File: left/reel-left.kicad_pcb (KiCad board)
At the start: 2 copper layers, 143.2 x 92.7 mm, 49 parts, among them J1 Conn_01x02, SW1 SW_Push, SW10 SW_Push, SW11 SW_Push, SW12 SW_Push, SW13 SW_Push, SW14 SW_Push, SW15 SW_Push, SW16 SW_Push, SW17 SW_Push, SW18 SW_Push, SW19 SW_Push, SW2 SW_Push, SW20 SW_Push, SW21 RotaryEncoder, SW22 SW_SPDT, SW3 SW_Push, SW4 SW_Push, SW5 SW_Push, SW6 SW_Push, SW7 SW_Push, SW8 SW_Push, SW9 SW_Push

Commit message: Update left PCB layout
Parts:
- added D21: D, Diode_SMD:D_SOD-123, F.Cu at (205.5, 115.8)
- added D22: D, Diode_SMD:D_SOD-123, F.Cu at (204.2, 118.0)
- added SW24: SW_SPDT, Button_Switch_SMD:SW_SPDT_PCM12, B.Cu at (208.3, 99.0)
- added SW25: RotaryEncoder, reel:RotaryEncoder_BM10_3Pin, F.Cu at (214.3, 122.9)
- SW21: value RotaryEncoder -> SW_Push; footprint reel:RotaryEncoder_BM10_3Pin -> reel:SideTactSwitch_2pin
- SW22: value SW_SPDT -> SW_Push; footprint Button_Switch_SMD:SW_SPDT_PCM12 -> reel:SideTactSwitch_2pin; moved to F.Cu
- moved SW22 45.8 mm to (202.0, 144.4), turned to 150 degrees
- moved SW21 3.93 mm to (216.7, 118.9)
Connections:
- SW22 pad 1: unconnected-(SW22-A-Pad1) -> Col1
- SW22 pad 2: Net-(J1-Pin_1) -> Net-(D22-A)
- U1 pad 15: unconnected-(U1-NFC1_0.09-Pad15) -> Row4
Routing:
- net Col1: track 193.8 -> 235.3 mm, vias 3 -> 4
- net Net-(D22-A): track 0.00 -> 28.9 mm
- net Net-(D21-A): track 0.00 -> 13.2 mm, vias 0 -> 1
- net Row4: track 0.00 -> 2.77 mm
- net unconnected-(SW24-A-Pad1): track 0.00 -> 0.65 mm
- net unconnected-(SW22-A-Pad1): track 0.65 -> 0.00 mm
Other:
- board size 143.2 x 92.7 mm -> 145.2 x 95 mm

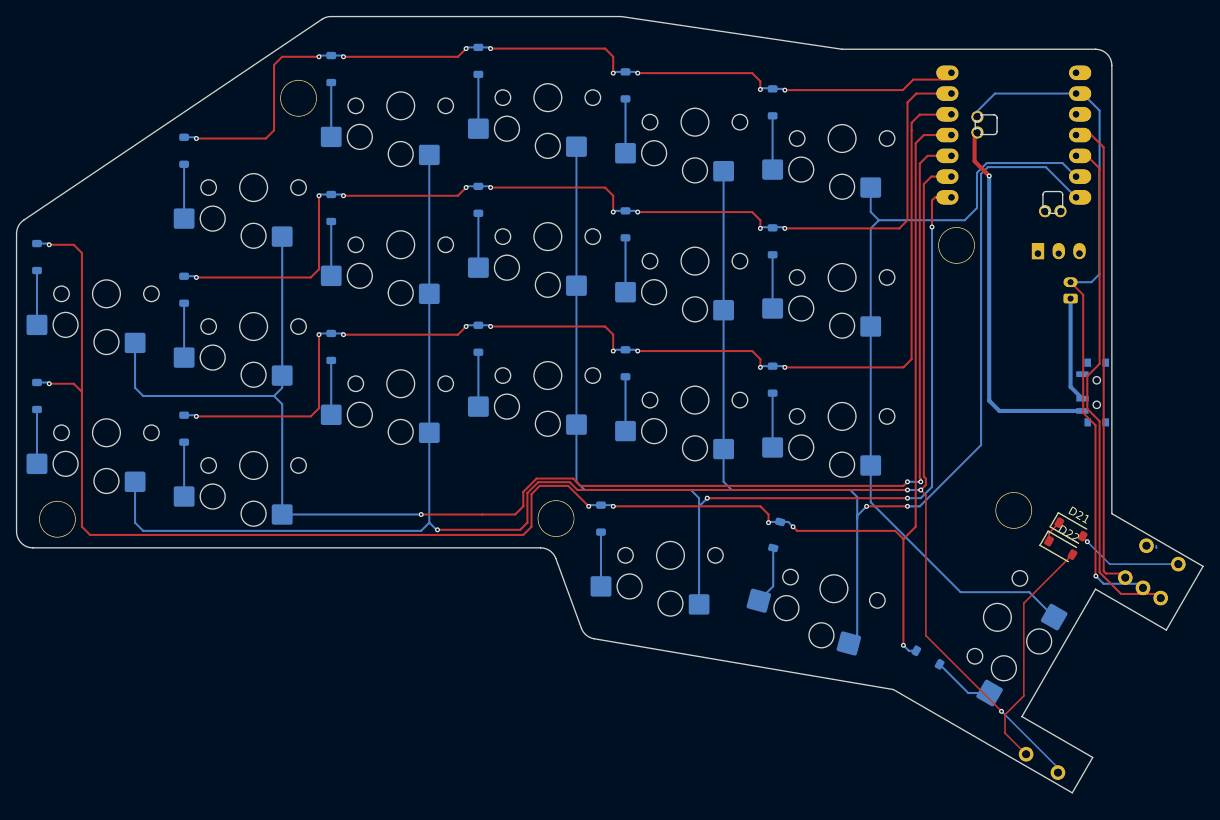
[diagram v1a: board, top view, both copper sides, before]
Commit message: Update left PCB layout
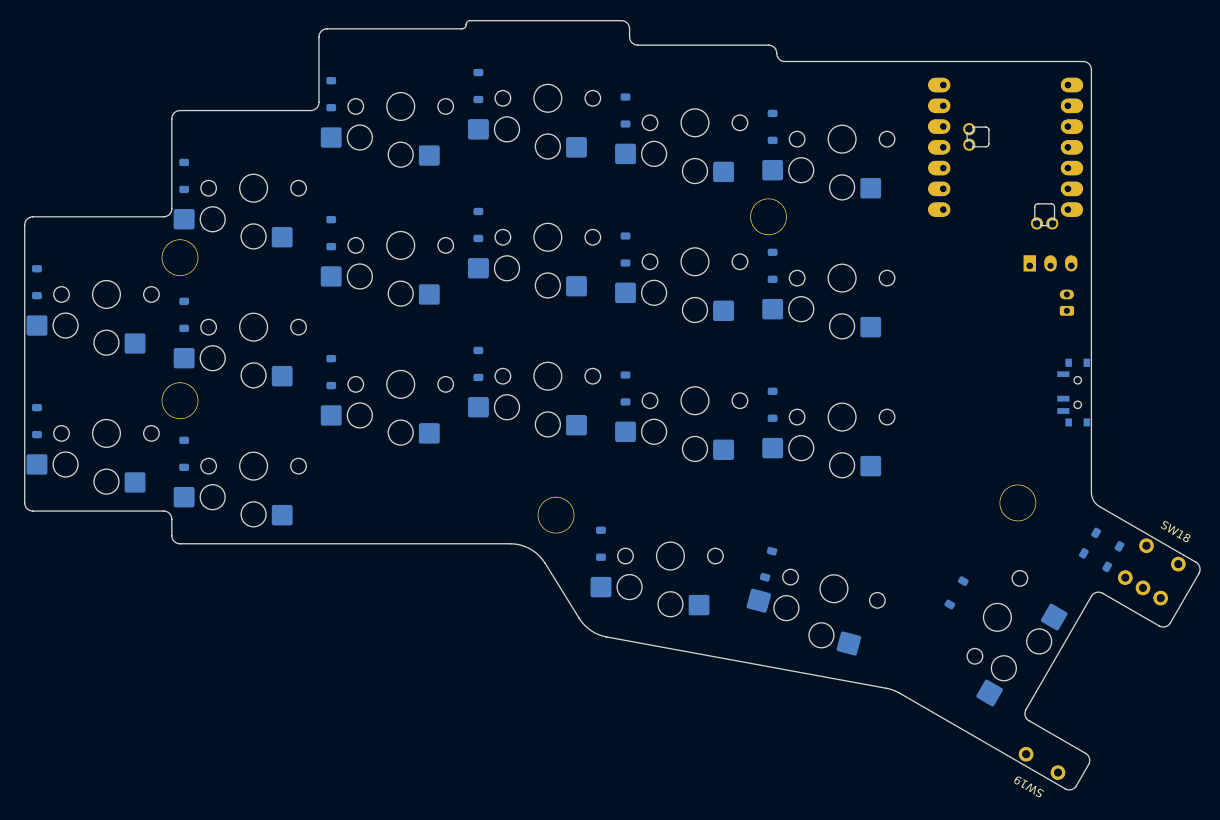
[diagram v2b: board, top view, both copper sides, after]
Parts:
- D21, D22: moved to B.Cu
- SW18, SW19: footprint reel:SW_Hotswap_Kailh_Choc_V1_1.00u-NoClickHole -> reel:SideTactSwitch_2pin
- SW21, SW22: footprint reel:SideTactSwitch_2pin -> reel:SW_Hotswap_Kailh_Choc_V1_1.00u-NoClickHole
- moved D10 72.6 mm to (97.0, 89.5)
- moved D5 72.6 mm to (97.0, 72.5)
- moved SW10 72.3 mm to (105.5, 91.0)
- moved SW5 72.3 mm to (105.5, 74.0)
- moved SW1 72.2 mm to (177.5, 68.0)
- moved SW6 72.2 mm to (177.5, 85.0)
- moved D1 72.1 mm to (169.0, 66.5)
- moved D6 72.1 mm to (169.0, 83.5)
- moved D18 62.1 mm to (210.0, 117.0), turned to -30 degrees
- moved SW18 60.2 mm to (216.7, 118.9), turned to -30 degrees
- moved D22 56.3 mm to (148.0, 117.5), turned to -90 degrees
- moved D12 54.5 mm to (169.0, 100.5)
- moved SW12 54.2 mm to (177.5, 102.0)
- moved SW15 54.1 mm to (123.5, 98.0)
- moved D15 54.0 mm to (115.0, 96.5)
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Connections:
- D11 pad 1: Row2 -> Row1
- D16 pad 1: Row3 -> Row2
- D17 pad 1: Row3 -> Row2
- D21 pad 1: Row4 -> Row3
- D22 pad 1: Row4 -> Row3
- SW11 pad 1: Col0 -> Col5
- SW12 pad 1: Col1 -> Col0
- SW13 pad 1: Col2 -> Col1
- SW14 pad 1: Col3 -> Col2
- SW15 pad 1: Col4 -> Col3
- SW16 pad 1: Col0 -> Col4
- SW17 pad 1: Col1 -> Col5
- SW18 pad 1: Col2 -> Col0
- SW19 pad 1: Col3 -> Col1
- SW20 pad 1: Col4 -> Col2
- SW21 pad 1: Col0 -> Col3
- SW22 pad 1: Col1 -> Col4
- U1 pad 15: Row4 -> Col5
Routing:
- net Col1: track 235.3 -> 0.00 mm, vias 4 -> 0
- net Row3: track 223.4 -> 0.00 mm, vias 7 -> 0
- net Col0: track 182.7 -> 0.00 mm, vias 3 -> 0
- net Col3: track 139.2 -> 0.00 mm, vias 2 -> 0
- net Row2: track 137.9 -> 0.00 mm, vias 9 -> 0
- net Col2: track 136.9 -> 0.00 mm, vias 3 -> 0
- net Row1: track 123.4 -> 0.00 mm, vias 9 -> 0
- net Row0: track 108.0 -> 0.00 mm, vias 9 -> 0
- net Col4: track 97.8 -> 0.00 mm
- net GND: track 85.0 -> 0.00 mm, vias 1 -> 0
- net RotB: track 63.4 -> 0.00 mm
- net RotA: track 59.3 -> 0.00 mm
- net VBAT_SW: track 45.1 -> 0.00 mm, vias 1 -> 0
- net Net-(D22-A): track 28.9 -> 0.00 mm
- net Net-(D21-A): track 13.2 -> 0.00 mm, vias 1 -> 0
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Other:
- board size 145.2 x 95 mm -> 143.8 x 94.1 mm

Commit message: Update left board assets
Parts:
- moved SW18 0.28 mm to (216.5, 119.1)
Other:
- board size 143.8 x 94.1 mm -> 144 x 94.5 mm
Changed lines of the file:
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@@
 	(generator_version "10.0")
 	(general
-		(thickness 1.49)
+		(thickness 1.69)
 		(legacy_teardrops no)
 	)
@@
 			(layer "dielectric 1"
 				(type "core")
-				(thickness 1.4)
+				(thickness 1.6)
 				(material "FR4")
 				(epsilon_r 4.5)
@@
 	(footprint "reel:SideTactSwitch_2pin"
 		(layer "F.Cu")
-		(at 216.685254 118.865029 -30)
+		(at 216.525 119.090674 -30)
 		(property "Reference" "SW18"
 			(at 0 -3.25 330)
@@
 		)
 		(fp_line
-			(start 0.250001 0)
+			(start 0.250001 0.000001)
 			(end 0.750003 -0.000001)
 			(stroke
@@
 	(gr_line
 		(start 148.681836 128.900131)
-		(end 182.917637 135.178698)
+		(end 182.2918 135.063925)
 		(stroke
 			(width 0.05)
@@
 		(layer "Edge.Cuts")
 	)
-	(gr_arc
-		(start 182.917637 135.178698)
-		(mid 183.741886 135.404098)
-		(end 184.515719 135.766552)
-		(stroke
-			(width 0.05)
-			(type default)
-		)
-		(layer "Edge.Cuts")
-	)
 	(gr_line
 		(start 200 137.778203)
@@
 	)
 	(gr_line
-		(start 204.794229 147.474355)
-		(end 184.515719 135.766552)
+		(start 204.544234 147.911373)
+		(end 182.291799 135.063924)
 		(stroke
 			(width 0.05)
@@
 	)
 	(gr_arc
-		(start 206.160254 147.10833)
-		(mid 205.553043 147.574261)
-		(end 204.794229 147.474355)
+		(start 205.91026 147.545346)
+		(mid 205.303048 148.011273)
+		(end 204.544234 147.911373)
 		(stroke
 			(width 0.05)
@@
 	)
 	(gr_line
-		(start 207.660254 144.510253)
-		(end 206.160254 147.10833)
+		(start 207.660254 144.514256)
+		(end 205.91026 147.545346)
 		(stroke
 			(width 0.05)
@@
 	(gr_line
 		(start 208 59.5)
-		(end 208 111.220089)
+		(end 208 111.797441)
 		(stroke
 			(width 0.05)
@@
 		(layer "Edge.Cuts")
 	)
-	(gr_arc
-		(start 209 112.95214)
-		(mid 208.267953 112.220088)
-		(end 208 111.220089)
-		(stroke
-			(width 0.05)
-			(type default)
-		)
-		(layer "Edge.Cuts")
-	)
-	(gr_line
-		(start 209 112.95214)
-		(end 220.794229 119.761542)
-		(stroke
-			(width 0.05)
-			(type solid)
-		)
-		(layer "Edge.Cuts")
-	)
 	(gr_line
 		(start 209.366025 123.555771)
@@
 	(gr_line
 		(start 217.660254 127.189746)
-		(end 221.160254 121.127567)
+		(end 221.410254 120.694555)
+		(stroke
+			(width 0.05)
+			(type solid)
+		)
+		(layer "Edge.Cuts")
+	)
+	(gr_line
+		(start 221.044229 119.32853)
+		(end 208.000001 111.797442)
 		(stroke
 			(width 0.05)
@@
 	)
 	(gr_arc
-		(start 220.794229 119.761542)
-		(mid 221.260155 120.368748)
-		(end 221.160254 121.127567)
+		(start 221.044229 119.32853)
+		(mid 221.510155 119.935736)
+		(end 221.410254 120.694555)
 		(stroke
 			(width 0.05)

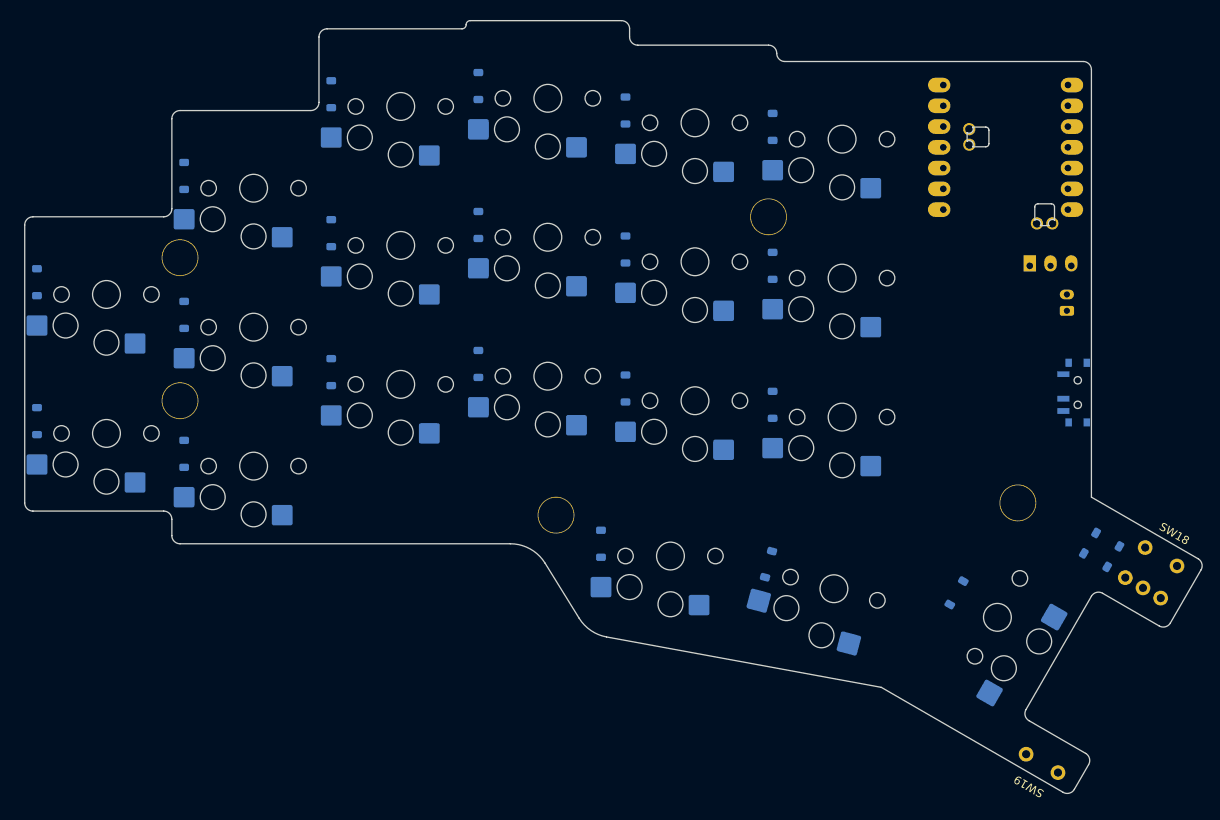
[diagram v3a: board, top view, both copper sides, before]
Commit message: Update ReeL KiCad libraries and board
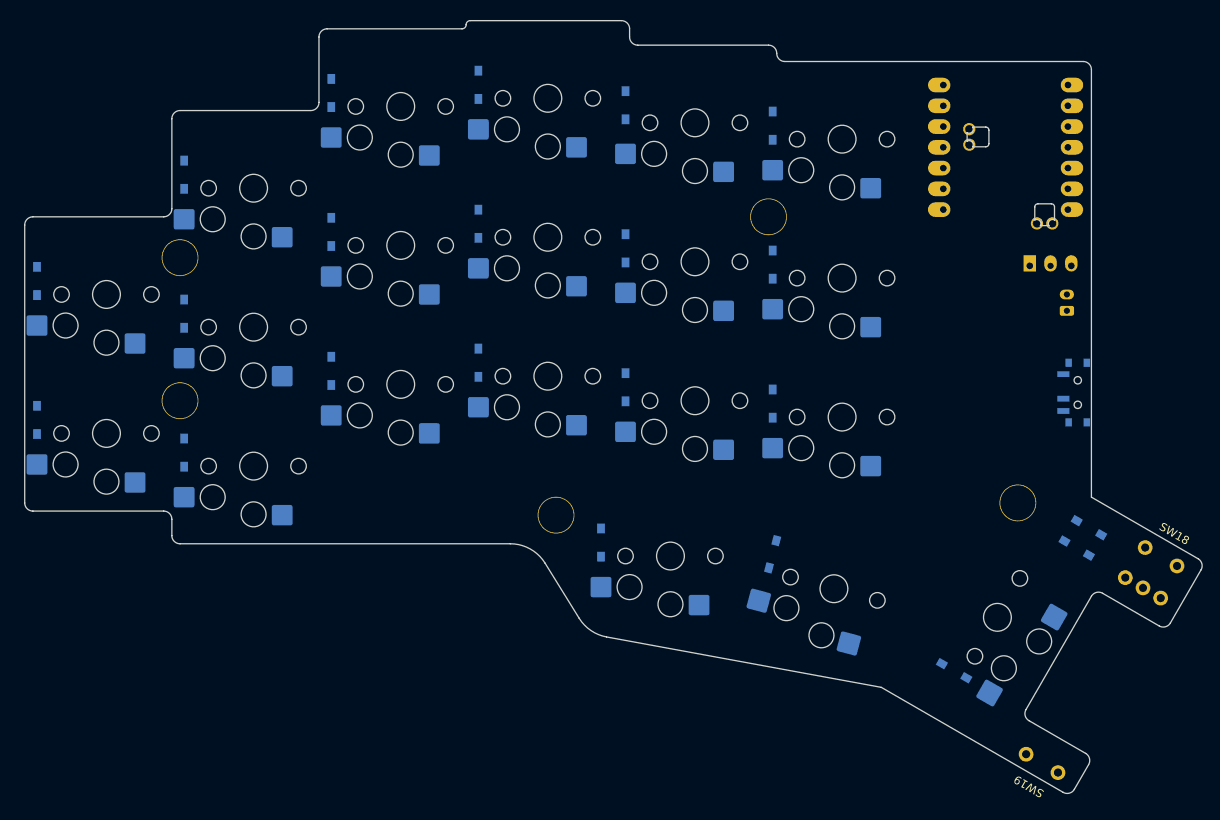
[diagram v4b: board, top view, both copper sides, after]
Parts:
- D1, D10, D11, D12, D13, D14, D15, D16, D17, D18, D19, D2, D20, D21, D22, D3, D4, D5, D6, D7, D8, D9: footprint Diode_SMD:D_SOD-123 -> reel:Diode_SMD; moved to F.Cu
- moved D20 8.58 mm to (188.8, 131.6), turned to -30 degrees
- moved D18 5.50 mm to (205.3, 114.1)
- moved D19 5.50 mm to (203.8, 116.6)
- moved D21 4.09 mm to (169.7, 116.1)
- moved D2 3.43 mm to (151.0, 61.1)
- moved D10 2.93 mm to (97.0, 86.6)
- moved D11 2.93 mm to (79.0, 82.6)
- moved D12 2.93 mm to (169.0, 97.6)
- moved D13 2.93 mm to (151.0, 95.6)
- moved D14 2.93 mm to (133.0, 92.6)
- moved D15 2.93 mm to (115.0, 93.6)
- moved D16 2.93 mm to (97.0, 103.6)
- moved D17 2.93 mm to (79.0, 99.6)
- moved D22 2.93 mm to (148.0, 114.6)
- moved D5 2.93 mm to (97.0, 69.6)
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
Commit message: Update ReeL KiCad board files
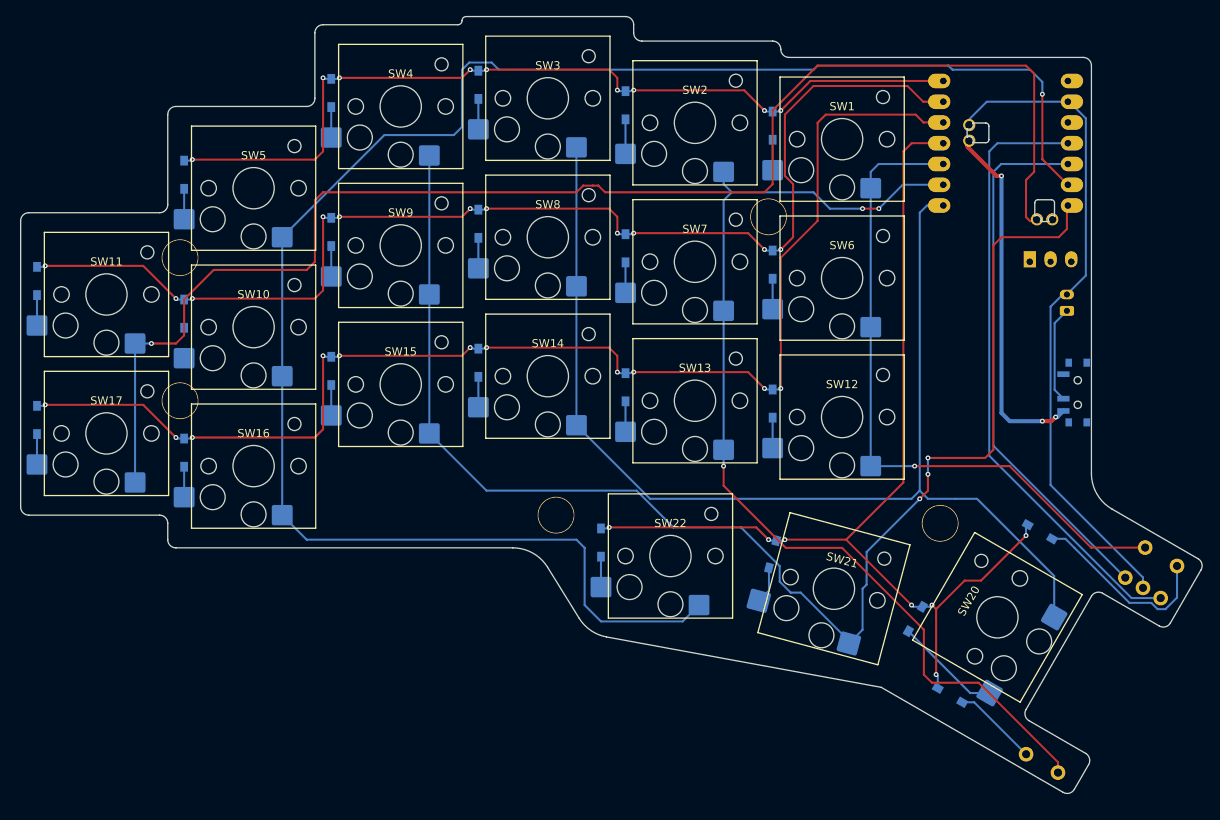
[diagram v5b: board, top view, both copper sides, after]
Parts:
- SW1, SW10, SW11, SW12, SW13, SW14, SW15, SW16, SW17, SW2, SW20, SW21, SW22, SW3, SW4, SW5, SW6, SW7, SW8, SW9: footprint reel:SW_Hotswap_Kailh_Choc_V1_1.00u-NoClickHole -> reel:SW_Hotswap_Kailh_Choc_V1V2_1.00u
- moved D19 23.8 mm to (188.3, 134.6)
- moved Ref** 9.82 mm to (189.5, 115.0)
- moved D20 7.41 mm to (187.9, 124.3), turned to -120 degrees
- moved D18 6.02 mm to (199.3, 114.6)
- moved U1 0.50 mm to (197.5, 58.0)
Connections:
- U1 pad 10: RotB -> RotA
- U1 pad 11: RotA -> RotB
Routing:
- net Col4: track 0.00 -> 216.5 mm, vias 0 -> 1
- net Col5: track 0.00 -> 173.7 mm, vias 0 -> 1
- net Col3: track 0.00 -> 170.2 mm, vias 0 -> 3
- net Row2: track 0.00 -> 156.9 mm, vias 0 -> 11
- net Row1: track 0.00 -> 146.3 mm, vias 0 -> 11
- net Col2: track 0.00 -> 143.2 mm
- net Row3: track 0.00 -> 127.2 mm, vias 0 -> 7
- net Col1: track 0.00 -> 126.6 mm, vias 0 -> 3
- net Row0: track 0.00 -> 107.6 mm, vias 0 -> 9
- net Col0: track 0.00 -> 83.0 mm, vias 0 -> 1
- net GND: track 0.00 -> 80.5 mm
- net RotB: track 0.00 -> 75.6 mm
- net RotA: track 0.00 -> 66.0 mm
- net VBAT_SW: track 0.00 -> 44.0 mm, vias 0 -> 3
- net Net-(D18-A): track 0.00 -> 23.5 mm
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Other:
- board size 144 x 94.5 mm -> 144.5 x 95 mm

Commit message: Update ReeL KiCad board files
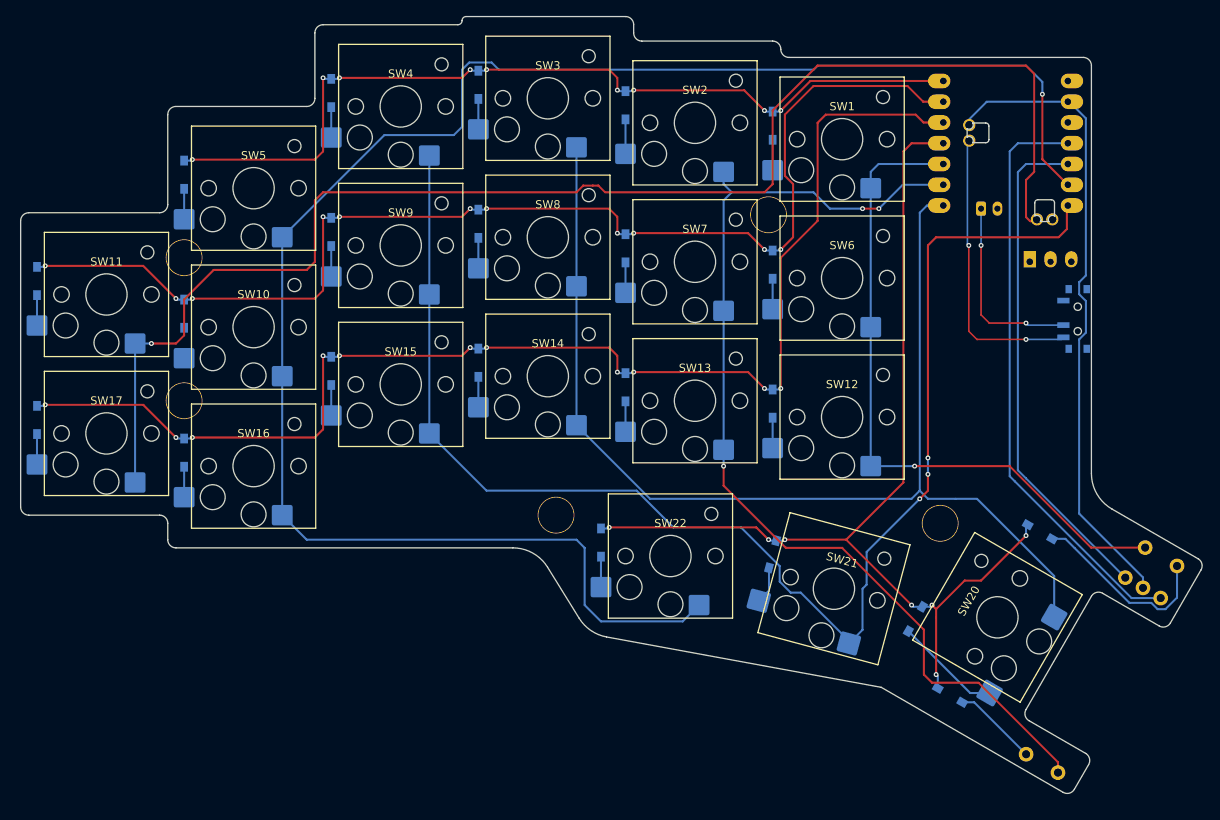
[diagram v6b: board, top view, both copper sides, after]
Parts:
- moved J1 16.3 mm to (194.5, 76.5), turned to 0 degrees
- moved SW24 9.00 mm to (206.0, 90.0)
- moved Ref** 0.50 mm to (97.0, 82.5)
- moved Ref** 0.50 mm to (97.0, 100.0)
- moved Ref** 0.25 mm to (168.5, 77.2)
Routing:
- net Net-(J1-Pin_1): track 11.8 -> 23.6 mm, vias 0 -> 2
- net VBAT_SW: track 44.0 -> 35.3 mm, vias 3 -> 2
- net RotA: track 66.0 -> 61.8 mm
- net RotB: track 75.6 -> 72.1 mm
- net GND: track 80.5 -> 78.0 mm
- net Col3: track 170.2 -> 170.7 mm

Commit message: Update PCB layouts and fabrication outputs
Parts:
- moved J1 6.80 mm to (196.5, 83.0), turned to 180 degrees
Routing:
- net GND: track 78.0 -> 101.2 mm
- net Net-(J1-Pin_1): track 23.6 -> 13.6 mm, vias 2 -> 1
- net Net-(D10-A): track 0.00 -> 3.72 mm
